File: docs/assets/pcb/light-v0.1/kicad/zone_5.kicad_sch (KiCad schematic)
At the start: 13 parts, among them J6 ZONE 5, Q113 AO3422, Q114 AO3422, Q115 AO3422

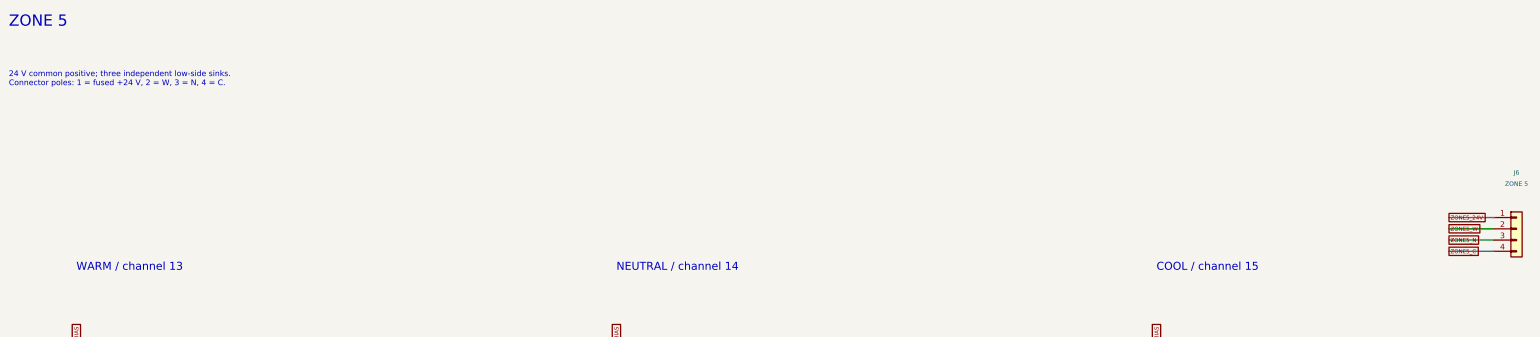
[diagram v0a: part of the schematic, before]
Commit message: Refresh PCB chapters from verified central LED snapshots
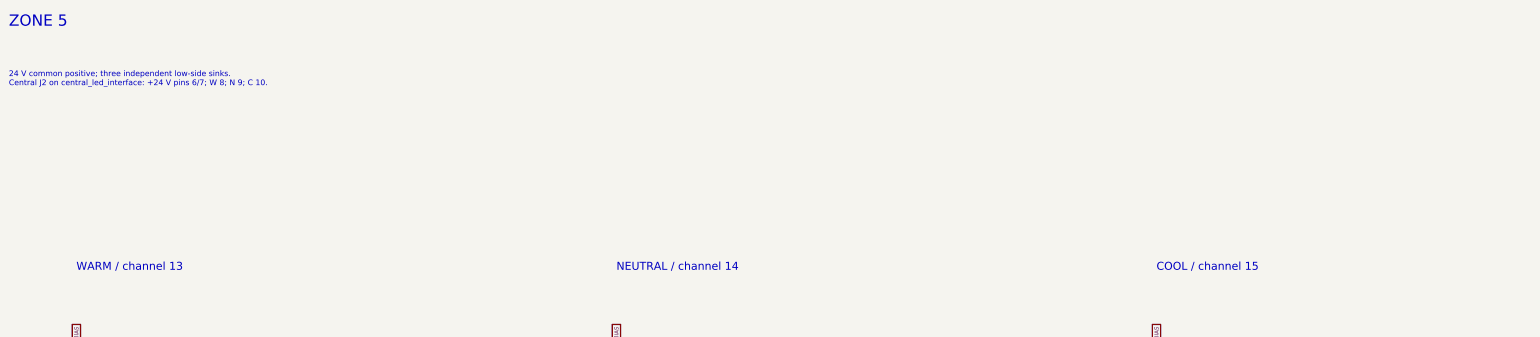
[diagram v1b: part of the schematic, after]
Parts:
- removed J6: ZONE 5, ELF:Enclosure_J6, symbol Connector_Generic:Conn_01x04
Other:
- note added: "24 V common positive; three independent low-side sinks. Central J2 on central_led_interface: +24 V pins 6/7; W 8; N 9; C 10."
- note removed: "24 V common positive; three independent low-side sinks. Connector poles: 1 = fused +24 V, 2 = W, 3 = N, 4 = C."
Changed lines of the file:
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@@
   (title_block
     (title "Zone 5")
-    (date "2026-09-06")
-    (rev "A draft")
+    (date "2026-09-08")
+    (rev "LIGHT v0.2 candidate")
     (company "Engineered Lighting")
     (comment 1 "ENGINEERING DRAFT - see release status before fabrication"))
-  (symbol
-    (lib_id "Connector_Generic:Conn_01x04")
-    (at 360.68 63.5 0)
-    (unit 1)
-    (exclude_from_sim yes)
-    (in_bom yes)
-    (on_board yes)
-    (dnp no)
-    (property "Reference" "J6"
-      (at 360.68 50.8 0.0)
-      (effects
-        (font
-          (size 1.0 1.0))))
-    (property "Value" "ZONE 5"
-      (at 360.68 53.34 0.0)
-      (effects
-        (font
-          (size 1.0 1.0))))
-    (property "Footprint" "ELF:Enclosure_J6"
-      (at 360.68 63.5 0.0)
-      (hide yes)
-      (effects
-        (font
-          (size 1.0 1.0))))
-    (property "MPN" "SM04B-GHS-TB(LF)(SN)"
-      (at 360.68 63.5 0.0)
-      (hide yes)
-      (effects
-        (font
-          (size 1.0 1.0))))
-    (property "Manufacturer" "JST"
-      (at 360.68 63.5 0.0)
-      (hide yes)
-      (effects
-        (font
-          (size 1.0 1.0))))
-    (property "Datasheet" ""
-      (at 360.68 63.5 0.0)
-      (hide yes)
-      (effects
-        (font
-          (size 1.0 1.0))))
-    (instances
-      (project "engineered-lighting-rev-a"
-        (path "/964013ac-cca6-5de7-b648-d598a25a58e0/65601d02-576b-5971-ab65-5ba7362ea97b"
-          (reference "J6")
-          (unit 1))))
-    (pin "1"
-)
-    (pin "2"
-)
-    (pin "3"
-)
-    (pin "4"
-))
-  (wire
-    (pts
-      (xy 355.6 60.96)
-      (xy 345.44 60.96))
-    (stroke
-      (width 0)
-      (type default))
-)
-  (global_label "ZONE5_24V"
-    (shape passive)
-    (at 345.44 60.96 0.0)
-    (effects
-      (font
-        (size 0.9 0.9))
-      (justify left))
-    (property "Intersheetrefs" "${INTERSHEET_REFS}"
-      (at 345.44 60.96 0.0)
-      (hide yes)
-      (effects
-        (font
-          (size 1.0 1.0)))))
-  (wire
-    (pts
-      (xy 355.6 63.5)
-      (xy 345.44 63.5))
-    (stroke
-      (width 0)
-      (type default))
-)
-  (global_label "ZONE5_W"
-    (shape passive)
-    (at 345.44 63.5 0.0)
-    (effects
-      (font
-        (size 0.9 0.9))
-      (justify left))
-    (property "Intersheetrefs" "${INTERSHEET_REFS}"
-      (at 345.44 63.5 0.0)
-      (hide yes)
-      (effects
-        (font
-          (size 1.0 1.0)))))
-  (wire
-    (pts
-      (xy 355.6 66.04)
-      (xy 345.44 66.04))
-    (stroke
-      (width 0)
-      (type default))
-)
-  (global_label "ZONE5_N"
-    (shape passive)
-    (at 345.44 66.04 0.0)
-    (effects
-      (font
-        (size 0.9 0.9))
-      (justify left))
-    (property "Intersheetrefs" "${INTERSHEET_REFS}"
-      (at 345.44 66.04 0.0)
-      (hide yes)
-      (effects
-        (font
-          (size 1.0 1.0)))))
-  (wire
-    (pts
-      (xy 355.6 68.58)
-      (xy 345.44 68.58))
-    (stroke
-      (width 0)
-      (type default))
-)
-  (global_label "ZONE5_C"
-    (shape passive)
-    (at 345.44 68.58 0.0)
-    (effects
-      (font
-        (size 0.9 0.9))
-      (justify left))
-    (property "Intersheetrefs" "${INTERSHEET_REFS}"
-      (at 345.44 68.58 0.0)
-      (hide yes)
-      (effects
-        (font
-          (size 1.0 1.0)))))
   (symbol
     (lib_id "EL:AO3422")
@@
       (justify left top))
 )
-  (text "24 V common positive; three independent low-side sinks.\nConnector poles: 1 = fused +24 V, 2 = W, 3 = N, 4 = C."
+  (text "24 V common positive; three independent low-side sinks.\nCentral J2 on central_led_interface: +24 V pins 6/7; W 8; N 9; C 10."
     (at 20.32 27.94 0)
     (effects
